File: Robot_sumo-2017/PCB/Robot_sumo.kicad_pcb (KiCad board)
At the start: 2 copper layers, 58 parts, among them J1 CONN_Batt, J2 CONN_C1, J3 CONN_C3, J4 CONN_C2, J5 CONN_C4, J6 CONN_M1, J7 CONN_M2, J8 CONN_distance, U1 Arduino-nano, U2 LM324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

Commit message: last version I hope
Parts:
- added G***: LOGO, logo:phelma-logo-exp2, B.Cu at (141.3, 126.1)
- added G***: LOGO, logo:phelma-logo, F.Cu at (118.3, 101.4)
- added U5: trou-3, Arduino-nano:Trou-3, F.Cu at (107.9, 177.0)
- added U6: trou-3, Arduino-nano:Trou-3, F.Cu at (171.9, 93.0)
- added U7: trou-3, Arduino-nano:Trou-3, F.Cu at (108.0, 93.0)
- moved R14 61.0 mm to (113.9, 105.7), turned to 0 degrees
- moved R15 56.0 mm to (117.6, 108.3), turned to 0 degrees
- moved D1 54.4 mm to (107.2, 98.9), turned to 0 degrees
- moved J2 53.0 mm to (169.9, 170.3), turned to 270 degrees
- moved R6 52.2 mm to (111.6, 168.0), turned to 180 degrees
- moved C3 50.3 mm to (116.3, 171.4), turned to 180 degrees
- moved C9 50.1 mm to (121.4, 111.8), turned to 270 degrees
- moved D2 49.8 mm to (111.6, 165.0), turned to 0 degrees
- moved Rlim1 48.3 mm to (158.7, 175.5), turned to 180 degrees
- moved U3 46.7 mm to (108.9, 119.6), turned to 90 degrees
- moved J4 45.1 mm to (169.9, 160.2), turned to 270 degrees
- moved Rmes1 44.9 mm to (158.8, 172.7), turned to 180 degrees
- moved U2 44.5 mm to (113.8, 161.4), turned to 90 degrees
- moved D5 42.0 mm to (111.9, 150.1), turned to 0 degrees
- moved R2 41.7 mm to (145.0, 175.4), turned to 180 degrees
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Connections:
- U1 pad 29: /distance_sensor/Trig -> /distance_sensor/Echo
- U1 pad 30: /distance_sensor/Echo -> /distance_sensor/Trig
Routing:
- net +5V: track 448.9 -> 315.0 mm, vias 5 -> 6
- net /R-IR/C1: track 68.7 -> 99.2 mm
- net Net-(R1-Pad2): track 32.7 -> 4.33 mm
- net /R-IR/C3: track 74.3 -> 56.5 mm
- net /motor-part/PWM1: track 15.5 -> 31.9 mm, vias 0 -> 2
- net /motor-part/PWM2: track 36.6 -> 47.4 mm
- net /motor-part/O2: track 50.0 -> 59.5 mm
- net /motor-part/O1: track 24.0 -> 15.6 mm
- net /distance_sensor/Echo: track 7.58 -> 13.4 mm
- net /R-IR/C4: track 59.2 -> 53.5 mm
- net VCC: track 63.6 -> 67.3 mm
- net /R-IR/Signal-e: track 97.8 -> 100.0 mm, vias 1 -> 3
- net /distance_sensor/Trig: track 7.58 -> 9.41 mm
- net /R-IR/C2: track 79.3 -> 77.7 mm, vias 1 -> 2
- net Net-(C6-Pad1): track 47.4 -> 48.5 mm
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- removed copper zone on B.Cu, net GND
- removed copper zone on F.Cu, net GND
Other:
- board outline added: 70 x 90 mm
- net class Default: clearance 0.254 -> 0.31
- rule trace_clearance: 0.254 -> 0.31
- board text added: "Robotronik"
- board text removed: "Robotronik-2017"

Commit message: last version I hope
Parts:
- moved C7 0.78 mm to (131.7, 167.0)
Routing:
- net GND: track 394.8 -> 395.6 mm
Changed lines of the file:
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@@
 (kicad_pcb (version 4) (host pcbnew 4.0.6-e0-6349~53~ubuntu16.04.1)
   (general
-    (links 0)
-    (no_connects 0)
-    (area 104.924999 89.924999 175.075001 180.075001)
+    (links 128)
+    (no_connects 2)
+    (area 104.924999 89.855 175.595 180.075001)
     (thickness 1.6)
     (drawings 5)
@@
   )
   (module Capacitors_THT:C_Rect_L7.0mm_W2.5mm_P5.00mm (layer F.Cu)
-    (at 130.95 166.88 270)
+    (at 131.72 167 270)
     (descr "C, Rect series, Radial, pin pitch=5.00mm, , length*width=7*2.5mm^2, Capacitor")
     (tags "C Rect series Radial pin pitch 5.00mm  length 7mm width 2.5mm Capacitor")
@@
   (gr_line (start 105 90) (end 105 180) (layer Edge.Cuts) (width 0.15))
   (gr_line (start 105 90) (end 175 90) (layer Edge.Cuts) (width 0.15))
-  (segment (start 130.95 171.88) (end 128.14 174.69) (width 0.5) (layer B.Cu) (net 1))
-  (segment (start 128.14 174.69) (end 126.83 174.69) (width 0.5) (layer B.Cu) (net 1))
+  (segment (start 131.72 172) (end 129.03 174.69) (width 0.5) (layer B.Cu) (net 1))
+  (segment (start 129.03 174.69) (end 126.83 174.69) (width 0.5) (layer B.Cu) (net 1))
   (segment (start 137.65 170.54) (end 148.09 170.54) (width 0.5) (layer F.Cu) (net 1))
   (segment (start 148.09 170.54) (end 150.15 172.6) (width 0.5) (layer F.Cu) (net 1))
@@
   (segment (start 114.57 147.73) (end 116.97 150.13) (width 0.5) (layer B.Cu) (net 4))
   (segment (start 114.57 147.42) (end 114.57 147.73) (width 0.5) (layer B.Cu) (net 4))
-  (segment (start 130.95 166.88) (end 130.150001 166.080001) (width 0.5) (layer B.Cu) (net 5))
-  (segment (start 130.150001 166.080001) (end 130.150001 165.500001) (width 0.5) (layer B.Cu) (net 5))
+  (segment (start 130.150001 165.500001) (end 130.220001 165.500001) (width 0.5) (layer B.Cu) (net 5))
+  (segment (start 130.220001 165.500001) (end 131.72 167) (width 0.5) (layer B.Cu) (net 5))
   (segment (start 130.150001 165.500001) (end 129.4 164.75) (width 0.5) (layer B.Cu) (net 5))
   (segment (start 126.45 159.127208) (end 126.46 159.137208) (width 0.5) (layer B.Cu) (net 5))

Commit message: plan de masse
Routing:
- added copper zone on B.Cu, net GND
- added copper zone on F.Cu, net GND
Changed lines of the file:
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@@
   (general
     (links 128)
-    (no_connects 2)
+    (no_connects 0)
     (area 104.924999 89.855 175.595 180.075001)
     (thickness 1.6)
@@
   (segment (start 119.014484 105.73545) (end 115.034484 105.73545) (width 0.5) (layer B.Cu) (net 54))
   (segment (start 115.034484 105.73545) (end 112.474484 108.29545) (width 0.5) (layer B.Cu) (net 54))
+  (zone (net 1) (net_name GND) (layer B.Cu) (hatch edge 0.508)
+    (connect_pads (clearance 1))
+    (min_thickness 0.4)
+    (fill yes (arc_segments 16) (thermal_gap 0.508) (thermal_bridge_width 0.508))
+    (polygon
+      (pts
+        (xy 105 180) (xy 105 90) (xy 175 90) (xy 175 180)
+      )
+    )
+  )
+  (zone (net 1) (net_name GND) (layer F.Cu) (hatch edge 0.508)
+    (connect_pads (clearance 1))
+    (min_thickness 0.4)
+    (fill yes (arc_segments 16) (thermal_gap 0.508) (thermal_bridge_width 0.508))
+    (polygon
+      (pts
+        (xy 105 180) (xy 105 90) (xy 175 90) (xy 175 180)
+      )
+    )
+  )
 )

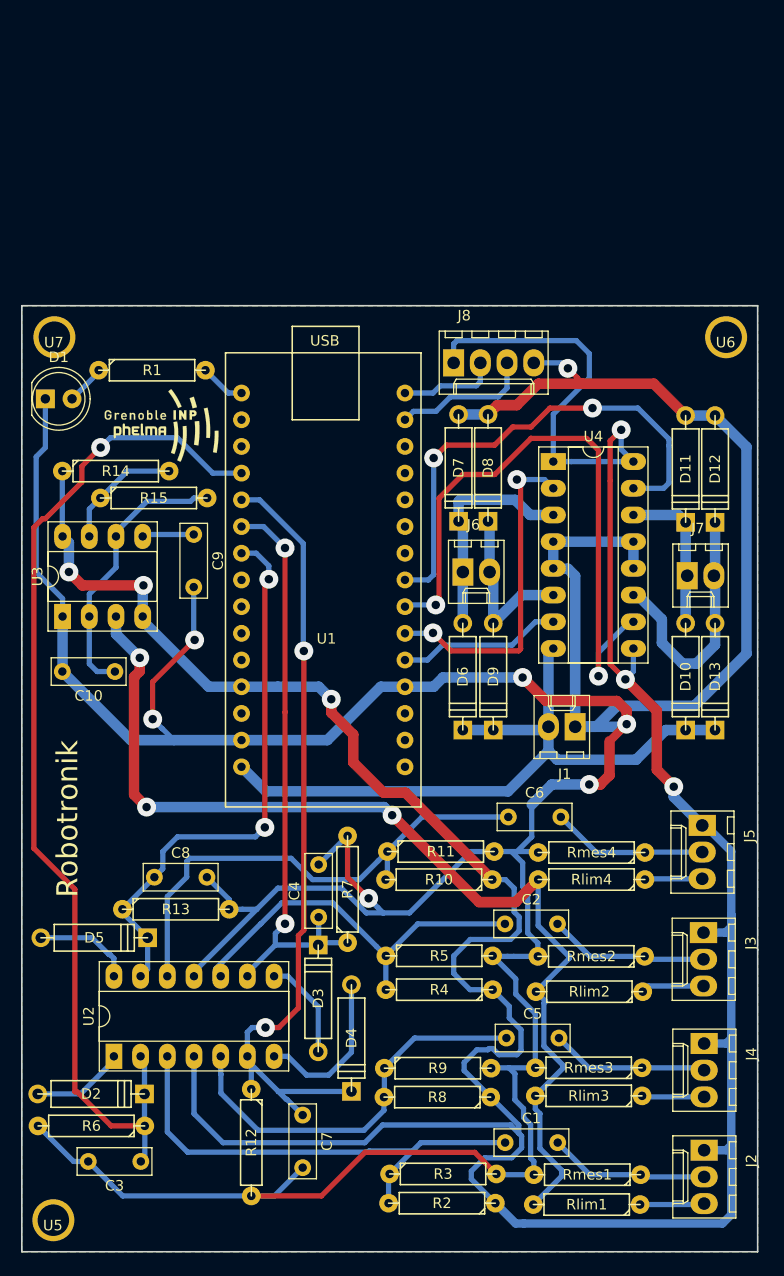
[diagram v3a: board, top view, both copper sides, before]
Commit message: changed some track under some capacitor and resistor
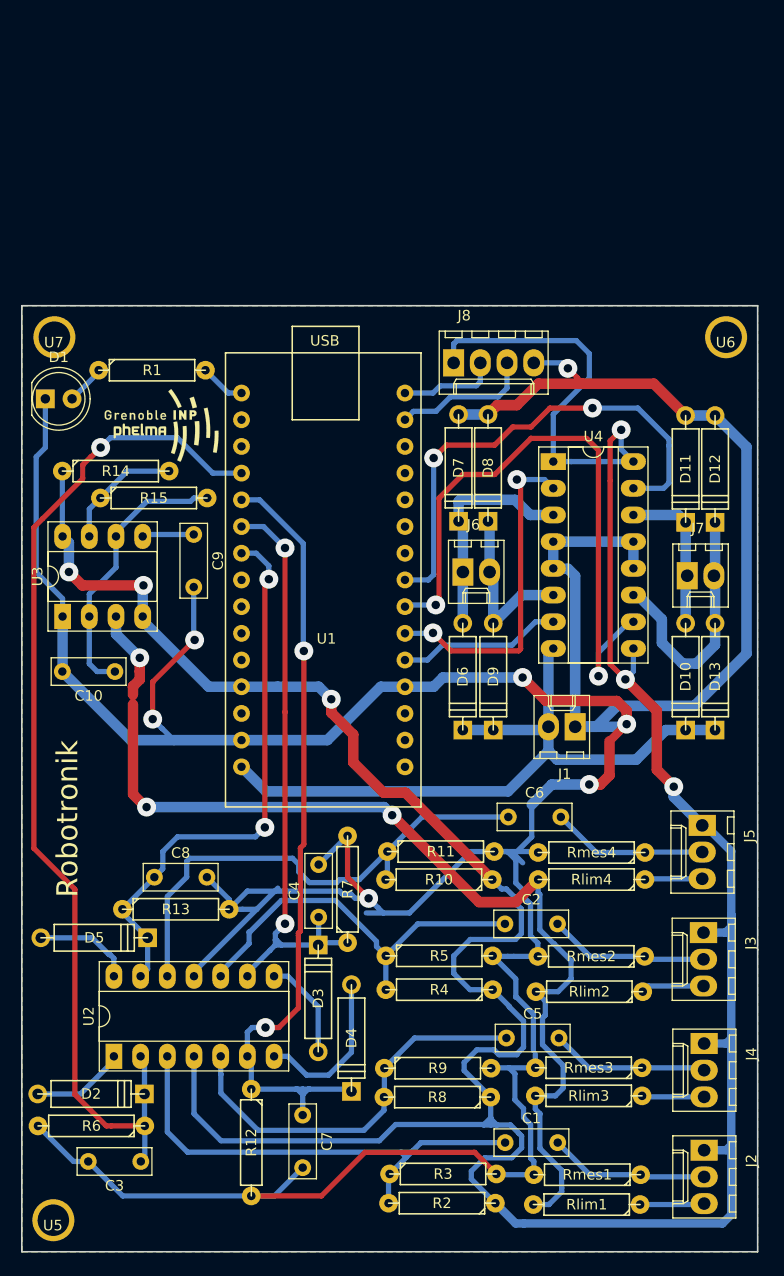
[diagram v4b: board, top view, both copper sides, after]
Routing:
- net GND: track 395.6 -> 403.0 mm
- net /R-IR/Signal-e: track 100.0 -> 103.5 mm
- net Net-(C2-Pad1): track 38.0 -> 39.2 mm
- net /R-IR/C3: track 56.5 -> 57.3 mm
- net Net-(C6-Pad1): track 48.5 -> 49.1 mm
- net /R-IR/C2: track 78.2 -> 77.6 mm
- net Net-(C1-Pad1): track 46.4 -> 47.0 mm

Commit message: added keepout area to erase copper pour glitch
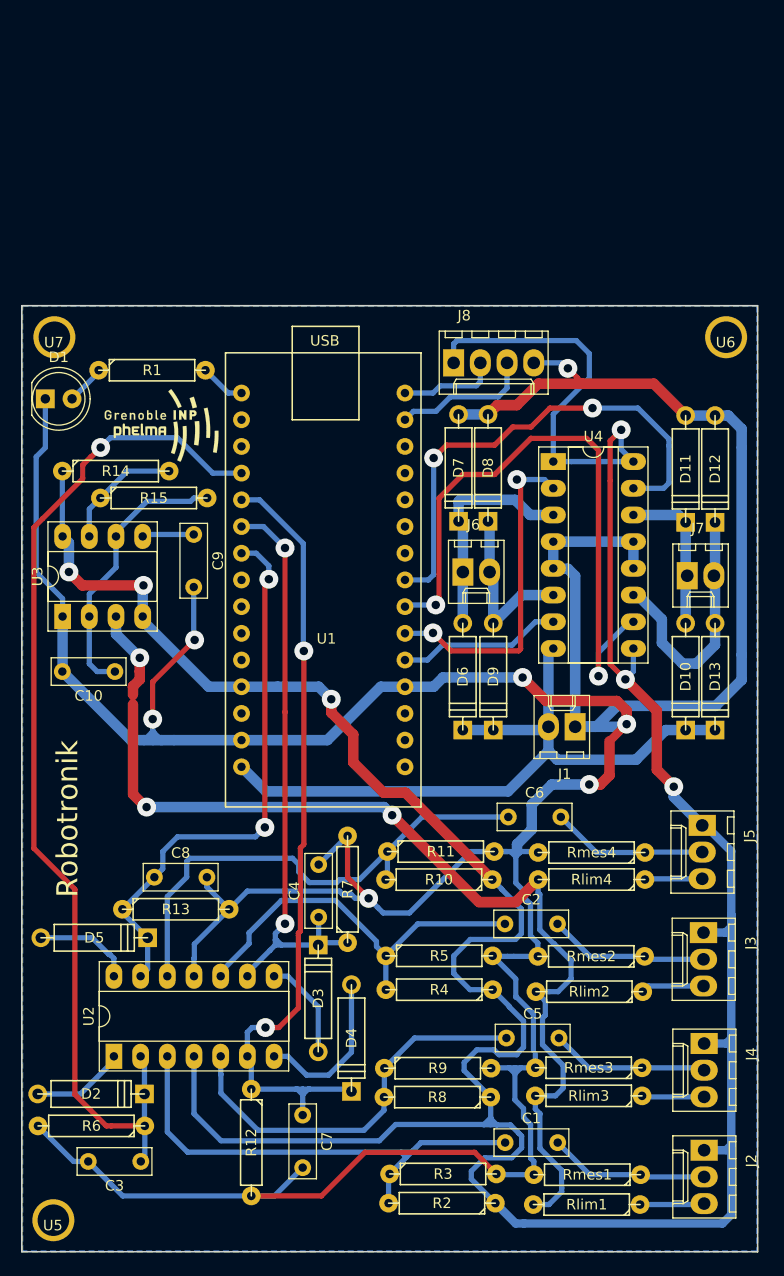
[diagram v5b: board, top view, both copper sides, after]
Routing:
- net GND: track 403.0 -> 399.5 mm

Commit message: changed area keepout shape + corrected a track width error
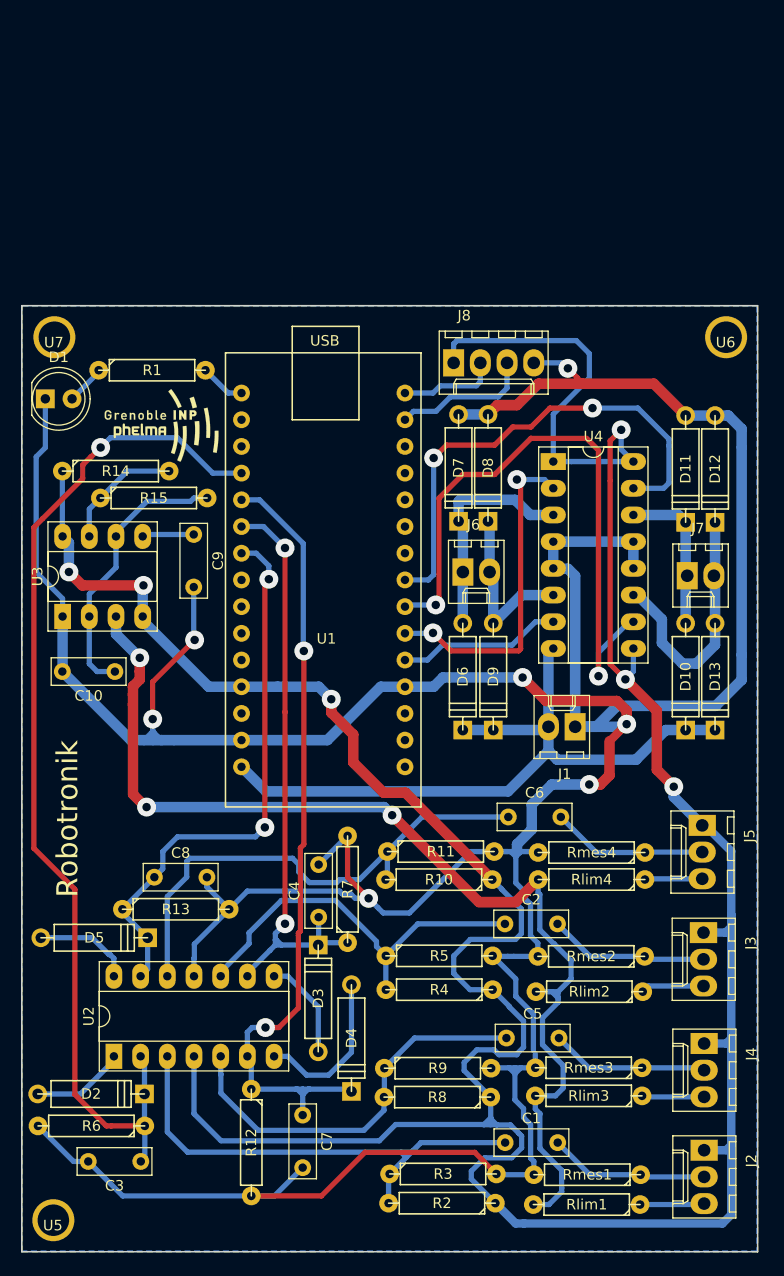
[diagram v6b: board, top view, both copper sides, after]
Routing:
- net /R-IR/Signal-e: track 103.5 -> 104.5 mm
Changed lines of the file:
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@@
     (thickness 1.6)
     (drawings 5)
-    (tracks 653)
+    (tracks 654)
     (zones 0)
     (modules 63)
@@
   (gr_line (start 105 90) (end 105 180) (layer Edge.Cuts) (width 0.15))
   (gr_line (start 105 90) (end 175 90) (layer Edge.Cuts) (width 0.15))
+  (segment (start 149.79 151.85) (end 151.99 154.05) (width 0.5) (layer B.Cu) (net 1))
+  (segment (start 151.99 155.6984) (end 153.58822 157.29662) (width 0.5) (layer B.Cu) (net 1))
+  (segment (start 151.99 154.05) (end 151.99 155.6984) (width 0.5) (layer B.Cu) (net 1))
+  (segment (start 153.58822 157.29662) (end 153.67 157.29662) (width 0.5) (layer B.Cu) (net 1))
+  (segment (start 153.67 157.29662) (end 153.67 160.8582) (width 0.5) (layer B.Cu) (net 1))
   (segment (start 115.379034 131.33) (end 116.6368 131.33) (width 1) (layer B.Cu) (net 1))
   (segment (start 116.6368 131.33) (end 117.4496 131.33) (width 1) (layer B.Cu) (net 1))
@@
   (segment (start 135.22681 145.69161) (end 126.45839 145.69161) (width 0.5) (layer B.Cu) (net 1))
   (segment (start 126.45839 145.69161) (end 124.73 147.42) (width 0.5) (layer B.Cu) (net 1))
-  (segment (start 152.0662 155.7746) (end 153.58822 157.29662) (width 0.5) (layer B.Cu) (net 1))
-  (segment (start 153.58822 157.29662) (end 153.67 157.29662) (width 0.5) (layer B.Cu) (net 1))
-  (segment (start 151.99 155.7746) (end 152.0662 155.7746) (width 0.5) (layer B.Cu) (net 1))
-  (segment (start 149.79 151.85) (end 151.99 154.05) (width 0.5) (layer B.Cu) (net 1))
-  (segment (start 151.99 154.05) (end 151.99 155.7746) (width 0.5) (layer B.Cu) (net 1))
-  (segment (start 153.67 157.29662) (end 153.67 160.8582) (width 0.5) (layer B.Cu) (net 1))
   (segment (start 153.85 161.19618) (end 153.85 162.5) (width 0.5) (layer B.Cu) (net 1))
   (segment (start 149.94 141.93) (end 151.197235 141.93) (width 0.5) (layer B.Cu) (net 1))
@@
   (segment (start 125.9 98.31) (end 124.64 98.31) (width 0.5) (layer B.Cu) (net 23))
   (segment (start 124.64 98.31) (end 122.47 96.14) (width 0.5) (layer B.Cu) (net 23))
+  (segment (start 155.4226 155.26) (end 155.167235 155.26) (width 0.5) (layer B.Cu) (net 24))
+  (segment (start 156.017 156.276) (end 156.017 155.8544) (width 0.5) (layer B.Cu) (net 24))
+  (segment (start 156.017 155.26) (end 155.4226 155.26) (width 0.5) (layer B.Cu) (net 24))
+  (segment (start 156.017 155.8544) (end 156.017 155.26) (width 0.5) (layer B.Cu) (net 24))
+  (segment (start 155.4226 155.26) (end 156.017 155.8544) (width 0.5) (layer B.Cu) (net 24))
+  (segment (start 153.85 165.17) (end 155.759 165.17) (width 0.5) (layer B.Cu) (net 24))
+  (segment (start 155.759 165.17) (end 156.5 164.429) (width 0.5) (layer B.Cu) (net 24))
+  (segment (start 156.5 164.429) (end 156.5 162.27) (width 0.5) (layer B.Cu) (net 24))
+  (segment (start 156.5 162.27) (end 154.5336 160.3036) (width 0.5) (layer B.Cu) (net 24))
+  (segment (start 154.5336 160.3036) (end 154.5336 157.7594) (width 0.5) (layer B.Cu) (net 24))
+  (segment (start 154.5336 157.7594) (end 156.017 156.276) (width 0.5) (layer B.Cu) (net 24))
   (segment (start 153.85 165.17) (end 153.85 166.427235) (width 0.5) (layer B.Cu) (net 24))
   (segment (start 156.35 172.24) (end 156.35 173.9262) (width 0.5) (layer B.Cu) (net 24))
@@
   (segment (start 156.3624 173.9386) (end 156.3624 174.2948) (width 0.5) (layer B.Cu) (net 24))
   (segment (start 156.3624 174.2948) (end 155.1472 175.51) (width 0.5) (layer B.Cu) (net 24))
-  (segment (start 154.5336 157.7594) (end 154.5336 160.3036) (width 0.5) (layer B.Cu) (net 24))
-  (segment (start 154.5336 160.3036) (end 156.5 162.27) (width 0.5) (layer B.Cu) (net 24))
-  (segment (start 154.798999 157.494001) (end 154.5336 157.7594) (width 0.5) (layer B.Cu) (net 24))
-  (segment (start 153.91 155.26) (end 154.798999 156.148999) (width 0.5) (layer B.Cu) (net 24))
-  (segment (start 154.798999 156.148999) (end 154.798999 157.494001) (width 0.5) (layer B.Cu) (net 24))
   (segment (start 157.2514 154.0256) (end 156.017 155.26) (width 0.5) (layer B.Cu) (net 24))
-  (segment (start 156.017 155.26) (end 155.167235 155.26) (width 0.5) (layer B.Cu) (net 24))
   (segment (start 157.2514 152.3238) (end 157.2514 154.0256) (width 0.5) (layer B.Cu) (net 24))
   (segment (start 155.633 150.7054) (end 157.2514 152.3238) (width 0.5) (layer B.Cu) (net 24))
@@
   (segment (start 154.2796 149.3774) (end 155.6076 150.7054) (width 0.5) (layer B.Cu) (net 24))
   (segment (start 155.167235 155.26) (end 153.91 155.26) (width 0.5) (layer B.Cu) (net 24))
-  (segment (start 155.759 165.17) (end 156.5 164.429) (width 0.5) (layer B.Cu) (net 24))
-  (segment (start 156.5 164.429) (end 156.5 162.27) (width 0.5) (layer B.Cu) (net 24))
-  (segment (start 153.85 165.17) (end 155.759 165.17) (width 0.5) (layer B.Cu) (net 24))
-  (segment (start 115.57 127) (end 115.57 127.9398) (width 0.5) (layer F.Cu) (net 24))
+  (segment (start 115.57 127) (end 115.57 127.9398) (width 1) (layer F.Cu) (net 24))
   (segment (start 116.22 125.5626) (end 115.57 126.2126) (width 1) (layer F.Cu) (net 24))
   (segment (start 115.57 126.2126) (end 115.57 127) (width 1) (layer F.Cu) (net 24))
@@
     )
   )
-  (zone (net 1) (net_name GND) (layer B.Cu) (hatch edge 0.508)
-    (connect_pads (clearance 1))
+  (zone (net 0) (net_name "") (layer B.Cu) (hatch full 0.508)
+    (connect_pads (clearance 0.508))
     (min_thickness 0.254)
-    (fill yes (arc_segments 16) (thermal_gap 0.508) (thermal_bridge_width 0.508))
+    (keepout (tracks allowed) (vias allowed) (copperpour not_allowed))
+    (fill (arc_segments 16) (thermal_gap 0.508) (thermal_bridge_width 0.508))
     (polygon
       (pts
-        (xy 105.0798 90.0684) (xy 174.9298 90.0684) (xy 174.9298 179.9336) (xy 105.0798 179.9336)
+        (xy 148.8948 148.7678) (xy 158.369 150.6474) (xy 158.4452 167.0304) (xy 145.669 167.1066) (xy 144.5768 152.5016)
+        (xy 147.9804 148.717)
       )
     )
   )
-  (zone (net 0) (net_name "") (layer B.Cu) (hatch full 0.508)
+  (zone (net 0) (net_name "") (layer B.Cu) (hatch edge 0.508)
     (connect_pads (clearance 0.508))
     (min_thickness 0.254)
@@
     (polygon
       (pts
-        (xy 148.1582 143.129) (xy 158.8262 143.2052) (xy 159.2326 174.1678) (xy 144.8054 174.0916) (xy 144.6784 148.5392)
-        (xy 148.8694 148.59)
+        (xy 149.0472 171.5262) (xy 156.1084 171.6532) (xy 156.1338 175.4632) (xy 149.4282 175.3616) (xy 148.4376 172.5168)
+        (xy 148.59 171.5262) (xy 149.0726 171.5262) (xy 149.1234 171.4754)
+      )
+    )
+  )
+  (zone (net 1) (net_name GND) (layer B.Cu) (hatch edge 0.508)
+    (connect_pads (clearance 1))
+    (min_thickness 0.254)
+    (fill yes (arc_segments 16) (thermal_gap 0.508) (thermal_bridge_width 0.508))
+    (polygon
+      (pts
+        (xy 105.0798 90.0684) (xy 174.9298 90.0684) (xy 174.9298 179.9336) (xy 105.0544 179.9336) (xy 105.0544 90.0684)
       )
     )
